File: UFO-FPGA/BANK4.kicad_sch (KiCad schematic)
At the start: 20 parts, among them SW1 SW_Push_DPDT, SW2 SW_DIP_x01, U1 ICE40HX8K-BG121

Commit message: Explainer
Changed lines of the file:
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@@
     (stroke (width 0) (type default))
   )
-  (rectangle (start 39.37 148.59) (end 99.06 177.8)
+  (rectangle (start 34.29 148.59) (end 106.68 177.8)
     (stroke (width 0) (type default))
     (fill (type none))
   )
+  (text_box "DOWN	For programming Flash - Shunt 1,3 and 2,4 (default)\nMOSI to MOSI & MISO to MISO\n\nUP		For programming iCE - Shunt 3,4 and 1,2\nMOSI to MISO & MISO to MOSI"
+    (at 34.29 177.8 0) (size 72.39 13.97)
+    (stroke (width 0) (type default))
+    (fill (type none))
+    (effects (font (size 1.27 1.27)) (justify left top))
+  )
   (label "ICE_MISO" (at 88.9 166.37 0) (fields_autoplaced)

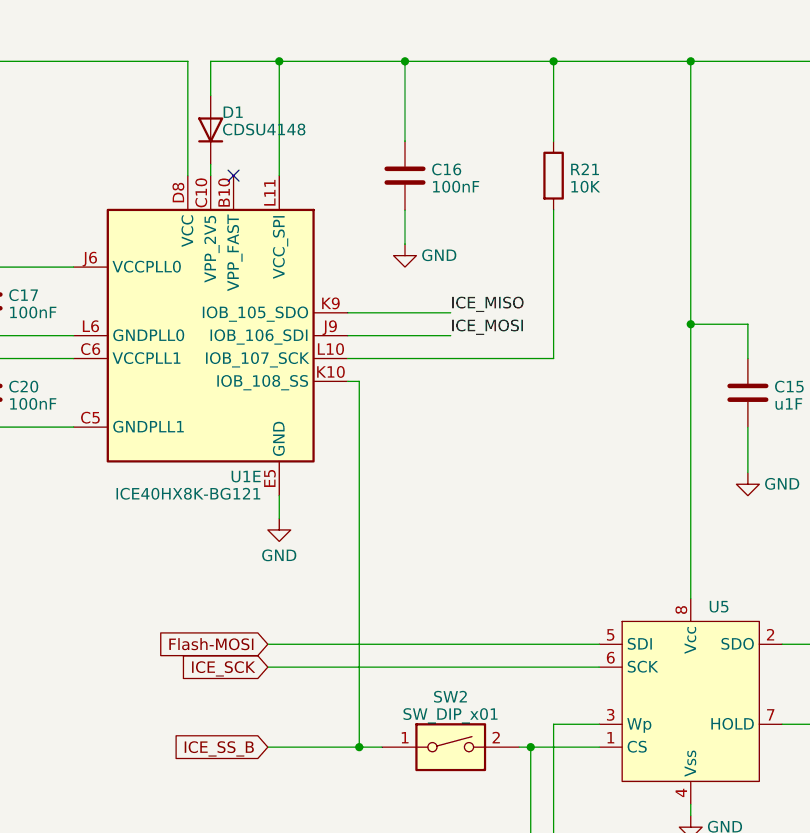
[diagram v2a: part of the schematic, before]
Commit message: Added net labels
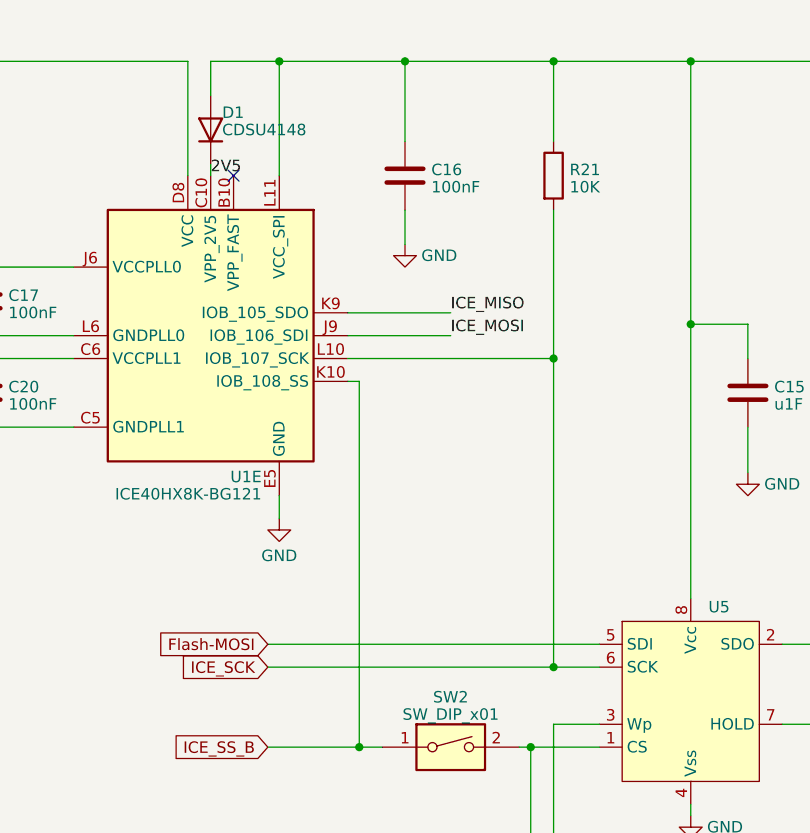
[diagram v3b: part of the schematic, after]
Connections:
- net ICE_SCK: now also R21.2, U1.L10 (IOB_107_SCK)
- net 2V5: now reaches D1.1 (K), U1.C10 (VPP_2V5)
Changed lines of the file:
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@@
   (junction (at 130.81 40.64) (diameter 0) (color 0 0 0 0)
   )
+  (junction (at 147.32 73.66) (diameter 0) (color 0 0 0 0)
+  )
   (junction (at 68.58 63.5) (diameter 0) (color 0 0 0 0)
   )
@@
   )
   (junction (at 147.32 40.64) (diameter 0) (color 0 0 0 0)
+  )
+  (junction (at 147.32 107.95) (diameter 0) (color 0 0 0 0)
   )
   (junction (at 73.66 73.66) (diameter 0) (color 0 0 0 0)
@@
     (stroke (width 0) (type default))
   )
-  (wire (pts (xy 115.57 107.95) (xy 152.4 107.95))
+  (wire (pts (xy 115.57 107.95) (xy 147.32 107.95))
     (stroke (width 0) (type default))
   )
@@
     (stroke (width 0) (type default))
   )
+  (wire (pts (xy 147.32 107.95) (xy 152.4 107.95))
+    (stroke (width 0) (type default))
+  )
   (wire (pts (xy 168.91 69.85) (xy 162.56 69.85))
     (stroke (width 0) (type default))
@@
   )
   (wire (pts (xy 147.32 57.15) (xy 147.32 73.66))
+    (stroke (width 0) (type default))
+  )
+  (wire (pts (xy 147.32 73.66) (xy 147.32 107.95))
     (stroke (width 0) (type default))
   )
@@
     (effects (font (size 1.27 1.27)) (justify left bottom))
   )
+  (label "2V5" (at 109.22 53.34 0) (fields_autoplaced)
+    (effects (font (size 1.27 1.27)) (justify left bottom))
+  )

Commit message: Labels and schametic changes
Updated Power schematic
Added labes for the different nets
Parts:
- removed U5: ~, symbol UFO_PARTS:N25Q032A13ESC40F
- added U9: N25Q032A13ESC40F, symbol UFO_PARTS:N25Q032A13ESC40F
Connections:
- net +3V3: now also U9.8 (Vcc)
- net Flash-MISO: now also U9.2 (SDO)
- net Flash-MOSI: now also U9.5 (SDI)
- net GND: now also U9.4 (Vss)
- net ICE_SCK: now also U9.6 (SCK)
- net VCCPLL0: now reaches C17.1, C18.1, R25.1, TP1.1, U1.J6 (VCCPLL0)
- net VCCPLL1: now reaches C19.1, C20.1, R26.2, TP1.1, U1.C6 (VCCPLL1)
- net N25-CS: now reaches R24.2, SW2.2
- net N25-CS: now also U9.1 (CS)
- net N25-WP: now reaches R23.2
- net N25-WP: now also U9.3 (Wp)
- net N25-HOLD: now reaches R22.2
- net N25-HOLD: now also U9.7 (HOLD)
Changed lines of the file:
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@@
+    (effects (font (size 1.27 1.27)) (justify left bottom))
+  )
+  (label "N25-CS" (at 149.225 133.35 0) (fields_autoplaced)
+    (effects (font (size 1.27 1.27)) (justify left bottom))
+  )
+  (label "VCCPLL1" (at 73.66 73.66 0) (fields_autoplaced)
     (effects (font (size 1.27 1.27)) (justify left bottom))
   )
@@
     (effects (font (size 1.27 1.27)) (justify left bottom))
   )
+  (label "N25-WP" (at 149.225 128.27 0) (fields_autoplaced)
+    (effects (font (size 1.27 1.27)) (justify left bottom))
+  )
+  (label "N25-HOLD" (at 176.53 114.3 0) (fields_autoplaced)
+    (effects (font (size 1.27 1.27)) (justify left bottom))
+  )
   (label "ICE_MOSI" (at 88.9 156.21 0) (fields_autoplaced)
+    (effects (font (size 1.27 1.27)) (justify left bottom))
+  )
+  (label "VCCPLL0" (at 73.66 63.5 0) (fields_autoplaced)
     (effects (font (size 1.27 1.27)) (justify left bottom))
   )
@@
         (path "/b3168f6a-c732-41d3-aeeb-d97dd2f1bb65/8a110dcf-7b5f-4510-96dd-3ef5ec8aca05"
           (reference "C42") (unit 1)
+        )
+      )
+    )
+  )
+  (symbol (lib_name "N25Q032A13ESC40F_1") (lib_id "UFO_PARTS:N25Q032A13ESC40F") (at 162.56 105.41 0) (unit 1)
+    (in_bom yes) (on_board yes) (dnp no) (fields_autoplaced)
+    (property "Reference" "U9" (at 164.5159 99.9871 0)
+      (effects (font (size 1.27 1.27)) (justify left))
+    )
+    (property "Value" "N25Q032A13ESC40F" (at 164.5159 101.9081 0)
+      (effects (font (size 1.27 1.27)) (justify left))
+    )
+    (property "Footprint" "" (at 146.05 121.285 0)
+      (effects (font (size 1.27 1.27)) hide)
+    )
+    (property "Datasheet" "" (at 146.05 121.285 0)
+      (effects (font (size 1.27 1.27)) hide)
+    )
+    (pin "4")
+    (pin "8")
+    (pin "1")
+    (pin "2")
+    (pin "3")
+    (pin "5")
+    (pin "6")
+    (pin "7")
+    (instances
+      (project "UFO-FPGA"
+        (path "/b3168f6a-c732-41d3-aeeb-d97dd2f1bb65/a9a0295d-b075-4952-a5ba-04debc5f691c"
+          (reference "U9") (unit 1)
         )
       )
@@
         )
       )
-    )
-  )
-  (symbol (lib_id "UFO_PARTS:N25Q032A13ESC40F") (at 162.56 105.41 0) (unit 1)
-    (in_bom yes) (on_board yes) (dnp no) (fields_autoplaced)
-    (property "Reference" "U5" (at 164.5159 101.2731 0)
-      (effects (font (size 1.27 1.27)) (justify left))
-    )
-    (property "Value" "~" (at 146.05 121.285 0)
-      (effects (font (size 1.27 1.27)))
-    )
-    (property "Footprint" "" (at 146.05 121.285 0)
-      (effects (font (size 1.27 1.27)) hide)
-    )
-    (property "Datasheet" "" (at 146.05 121.285 0)
-      (effects (font (size 1.27 1.27)) hide)
-    )
-    (pin "4")
-    (pin "8")
-    (pin "1")
-    (pin "2")
-    (pin "3")
-    (pin "5")
-    (pin "6")
-    (pin "7")
-    (instances
-      (project "UFO-FPGA"
-        (path "/b3168f6a-c732-41d3-aeeb-d97dd2f1bb65/a9a0295d-b075-4952-a5ba-04debc5f691c"
-          (reference "U5") (unit 1)
-        )
-        (path "/b3168f6a-c732-41d3-aeeb-d97dd2f1bb65/8a110dcf-7b5f-4510-96dd-3ef5ec8aca05"
-          (reference "U7") (unit 1)
-        )
-      )

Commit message: Revision
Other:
- company: (none) -> Universal-Field-Objects
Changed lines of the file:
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@@
   (paper "A4")
   (title_block
-    (date "2023-04-22")
-    (rev "V0.1")
+    (date "2023-04-25")
+    (rev "V0.5")
+    (company "Universal-Field-Objects")
   )
   (junction (at 125.73 116.84) (diameter 0) (color 0 0 0 0)

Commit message: PCB and footprint
Added foorprints and moved on pcb layout
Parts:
- C15: value u1F -> 100nF
- U9: footprint (none) -> Package_SO:SOP-8_3.9x4.9mm_P1.27mm
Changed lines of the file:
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@@
       (effects (font (size 1.27 1.27)) (justify left))
     )
-    (property "Value" "u1F" (at 171.831 78.7473 0)
+    (property "Value" "100nF" (at 171.831 78.7473 0)
       (effects (font (size 1.27 1.27)) (justify left))
     )
@@
       (effects (font (size 1.27 1.27)) (justify left))
     )
-    (property "Footprint" "" (at 146.05 121.285 0)
+    (property "Footprint" "Package_SO:SOP-8_3.9x4.9mm_P1.27mm" (at 146.05 121.285 0)
       (effects (font (size 1.27 1.27)) hide)
     )

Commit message: footprints and PCB
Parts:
- R21, R22, R23, R24, R25, R26: footprint (none) -> Resistor_SMD:R_0805_2012Metric_Pad1.20x1.40mm_HandSolder
- SW2: footprint (none) -> Button_Switch_SMD:SW_DIP_SPSTx01_Slide_9.78x4.72mm_W8.61mm_P2.54mm
- TP1: footprint (none) -> TestPoint:TestPoint_Keystone_5000-5004_Miniature
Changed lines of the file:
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@@
       (effects (font (size 1.27 1.27)))
     )
-    (property "Footprint" "" (at 135.89 116.84 0)
+    (property "Footprint" "Button_Switch_SMD:SW_DIP_SPSTx01_Slide_9.78x4.72mm_W8.61mm_P2.54mm" (at 135.89 116.84 0)
       (effects (font (size 1.27 1.27)) hide)
     )
@@
       (effects (font (size 1.27 1.27)) (justify left))
     )
-    (property "Footprint" "" (at 211.582 60.96 90)
+    (property "Footprint" "Resistor_SMD:R_0805_2012Metric_Pad1.20x1.40mm_HandSolder" (at 211.582 60.96 90)
       (effects (font (size 1.27 1.27)) hide)
     )
@@
       (effects (font (size 1.27 1.27)) (justify left))
     )
-    (property "Footprint" "" (at 63.5 63.5 0)
+    (property "Footprint" "TestPoint:TestPoint_Keystone_5000-5004_Miniature" (at 63.5 63.5 0)
       (effects (font (size 1.27 1.27)) hide)
     )
@@
       (effects (font (size 1.27 1.27)))
     )
-    (property "Footprint" "" (at 52.07 77.47 0)
+    (property "Footprint" "TestPoint:TestPoint_Keystone_5000-5004_Miniature" (at 52.07 77.47 0)
       (effects (font (size 1.27 1.27)) hide)
     )
@@
       (effects (font (size 1.27 1.27)))
     )
-    (property "Footprint" "" (at 55.88 65.278 90)
+    (property "Footprint" "Resistor_SMD:R_0805_2012Metric_Pad1.20x1.40mm_HandSolder" (at 55.88 65.278 90)
       (effects (font (size 1.27 1.27)) hide)
     )
@@
       (effects (font (size 1.27 1.27)) (justify left))
     )
-    (property "Footprint" "" (at 219.202 60.96 90)
+    (property "Footprint" "Resistor_SMD:R_0805_2012Metric_Pad1.20x1.40mm_HandSolder" (at 219.202 60.96 90)
       (effects (font (size 1.27 1.27)) hide)
     )
@@
       (effects (font (size 1.27 1.27)) (justify left))
     )
-    (property "Footprint" "" (at 203.962 60.96 90)
+    (property "Footprint" "Resistor_SMD:R_0805_2012Metric_Pad1.20x1.40mm_HandSolder" (at 203.962 60.96 90)
       (effects (font (size 1.27 1.27)) hide)
     )
@@
       (effects (font (size 1.27 1.27)) (justify right))
     )
-    (property "Footprint" "" (at 68.58 77.47 0)
+    (property "Footprint" "TestPoint:TestPoint_Keystone_5000-5004_Miniature" (at 68.58 77.47 0)
       (effects (font (size 1.27 1.27)) hide)
     )
@@
       (effects (font (size 1.27 1.27)) (justify left))
     )
-    (property "Footprint" "" (at 145.542 53.34 90)
+    (property "Footprint" "Resistor_SMD:R_0805_2012Metric_Pad1.20x1.40mm_HandSolder" (at 145.542 53.34 90)
       (effects (font (size 1.27 1.27)) hide)
     )
@@
       (effects (font (size 1.27 1.27)))
     )
-    (property "Footprint" "" (at 55.88 79.248 90)
-      (effects (font (size 1.27 1.27)) hide)
-    )
+    (property "Footprint" "Resistor_SMD:R_0805_2012Metric_Pad1.20x1.40mm_HandSolder" (at 55.88 79.248 90)
+      (effects (font (size 1.27 1.27)) hide)
+    )

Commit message: footprint
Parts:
- C15, C16, C17, C18, C19, C20: footprint (none) -> Capacitor_SMD:C_0805_2012Metric_Pad1.18x1.45mm_HandSolder
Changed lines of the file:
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@@
       (effects (font (size 1.27 1.27)) (justify left))
     )
-    (property "Footprint" "" (at 169.8752 81.28 0)
+    (property "Footprint" "Capacitor_SMD:C_0805_2012Metric_Pad1.18x1.45mm_HandSolder" (at 169.8752 81.28 0)
       (effects (font (size 1.27 1.27)) hide)
     )
@@
       (effects (font (size 1.27 1.27)) (justify left))
     )
-    (property "Footprint" "" (at 84.7852 71.12 0)
+    (property "Footprint" "Capacitor_SMD:C_0805_2012Metric_Pad1.18x1.45mm_HandSolder" (at 84.7852 71.12 0)
       (effects (font (size 1.27 1.27)) hide)
     )
@@
       (effects (font (size 1.27 1.27)) (justify left))
     )
-    (property "Footprint" "" (at 84.7852 81.28 0)
+    (property "Footprint" "Capacitor_SMD:C_0805_2012Metric_Pad1.18x1.45mm_HandSolder" (at 84.7852 81.28 0)
       (effects (font (size 1.27 1.27)) hide)
     )
@@
       (effects (font (size 1.27 1.27)) (justify left))
     )
-    (property "Footprint" "" (at 131.7752 57.15 0)
+    (property "Footprint" "Capacitor_SMD:C_0805_2012Metric_Pad1.18x1.45mm_HandSolder" (at 131.7752 57.15 0)
       (effects (font (size 1.27 1.27)) hide)
     )
@@
       (effects (font (size 1.27 1.27)) (justify left))
     )
-    (property "Footprint" "" (at 74.6252 71.12 0)
+    (property "Footprint" "Capacitor_SMD:C_0805_2012Metric_Pad1.18x1.45mm_HandSolder" (at 74.6252 71.12 0)
       (effects (font (size 1.27 1.27)) hide)
     )
@@
       (effects (font (size 1.27 1.27)) (justify left))
     )
-    (property "Footprint" "" (at 74.6252 81.28 0)
-      (effects (font (size 1.27 1.27)) hide)
-    )
+    (property "Footprint" "Capacitor_SMD:C_0805_2012Metric_Pad1.18x1.45mm_HandSolder" (at 74.6252 81.28 0)
+      (effects (font (size 1.27 1.27)) hide)
+    )
